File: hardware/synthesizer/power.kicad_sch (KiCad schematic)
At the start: 10 parts, among them U1 MAX40200ANS, U5 AP2112K-3.3

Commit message: update synthesizer
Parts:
- removed D5: BLUE_LED, symbol Device:LED
- removed R4: 1k, symbol Device:R
- added C12, C13: 1uF/16V, symbol Device:C
- added C14: 100uF/6.3V, symbol Device:C_Polarized
- added D8: Blue, symbol Device:LED
- added D9: Orange, symbol Device:LED
- added R13, R14: 1k, symbol Device:R
- added TP3: TestPoint, symbol Connector:TestPoint
- added U?: AP2112K-1.2, Package_TO_SOT_SMD:SOT-23-5, symbol Regulator_Linear:AP2112K-1.2
- D6: value RED_LED -> Red
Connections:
- net +5V: now also C12.1, R13.2, U?.1 (VIN), U?.3 (EN)
- net GND: now also C12.2, C13.2, C14.2, D8.1 (K), D9.1 (K), U?.2 (GND)
- new net: D9.2 (A), R14.2
- new net: D8.2 (A), R13.1
- new net +1.2V: C13.1, C14.1, R14.1, TP3.1, U?.5 (VOUT)
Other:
- note added: "5V -> 1.2V LDO"
- note added: "Power Led"

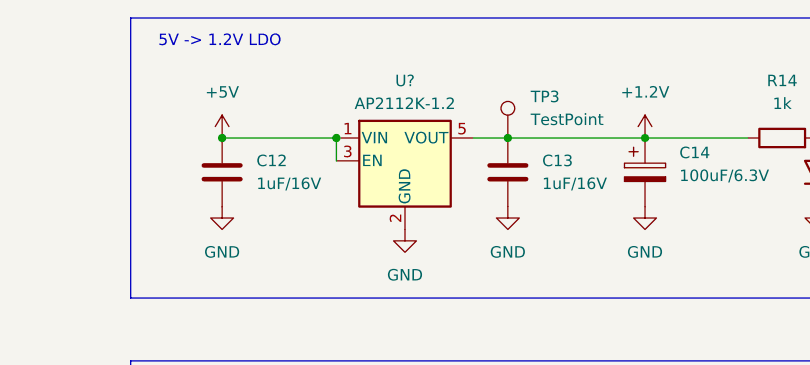
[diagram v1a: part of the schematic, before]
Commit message: finish ethernet jack
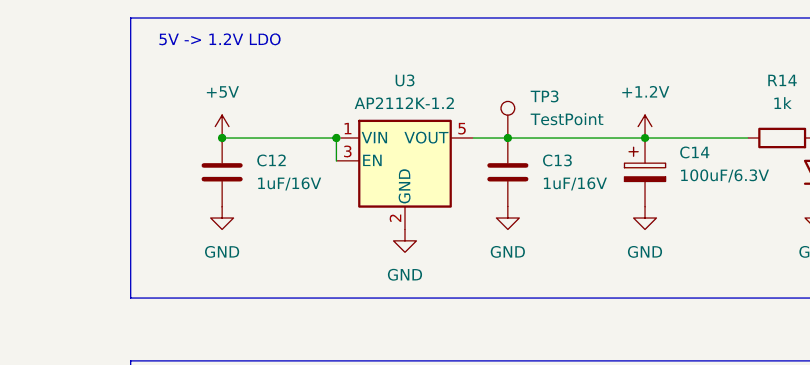
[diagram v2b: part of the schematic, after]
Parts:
- gave numbers to parts that had none: 1
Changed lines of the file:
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@@
 		(dnp no)
 		(fields_autoplaced yes)
-		(property "Reference" "U?"
+		(property "Reference" "U3"
 			(at 119.38 38.1 0)
 			(effects
@@
 			(project ""
 				(path "/f8740766-88d0-4c4d-b661-742f36f22c7b/9334189d-3538-4d48-bdb6-b549e4e68e82"
-					(reference "U?")
+					(reference "U3")
 					(unit 1)
 				)

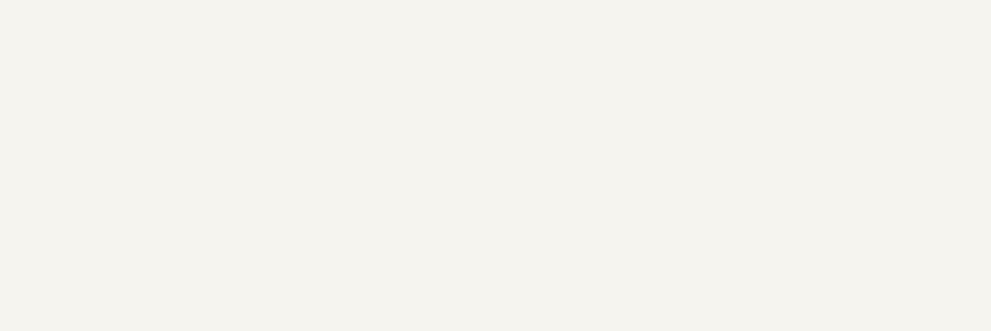
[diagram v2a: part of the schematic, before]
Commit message: add logo to every sheet
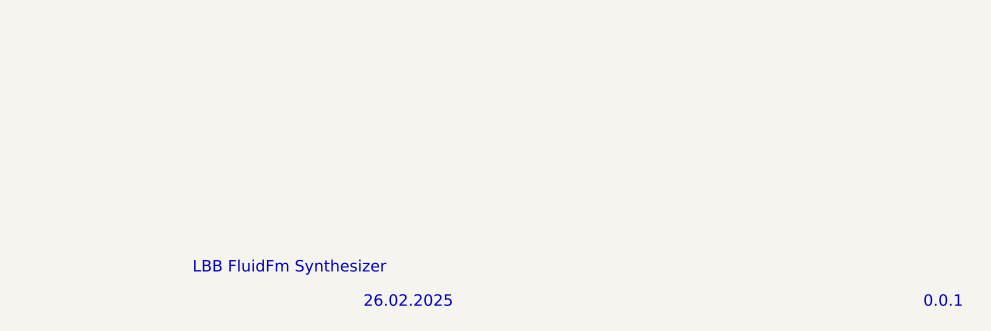
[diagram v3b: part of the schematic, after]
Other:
- note added: "0.0.1"
- note added: "26.02.2025"
- note added: "LBB FluidFm Synthesizer"

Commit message: improved pcb design
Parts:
- D6, D8, D9: footprint (none) -> LED_SMD:LED_0201_0603Metric
- R13, R14, R6: footprint (none) -> Resistor_SMD:R_0603_1608Metric
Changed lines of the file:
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@@
 			)
 		)
-		(property "Footprint" ""
+		(property "Footprint" "LED_SMD:LED_0201_0603Metric"
 			(at 165.1 86.36 0)
 			(effects
@@
 			)
 		)
-		(property "Footprint" ""
+		(property "Footprint" "Resistor_SMD:R_0603_1608Metric"
 			(at 161.29 84.328 90)
 			(effects
@@
 			)
 		)
-		(property "Footprint" ""
+		(property "Footprint" "LED_SMD:LED_0201_0603Metric"
 			(at 165.1 48.26 0)
 			(effects
@@
 			)
 		)
-		(property "Footprint" ""
+		(property "Footprint" "Resistor_SMD:R_0603_1608Metric"
 			(at 57.15 84.328 90)
 			(effects
@@
 			)
 		)
-		(property "Footprint" ""
+		(property "Footprint" "LED_SMD:LED_0201_0603Metric"
 			(at 49.53 87.63 0)
 			(effects
@@
 			)
 		)
-		(property "Footprint" ""
+		(property "Footprint" "Resistor_SMD:R_0603_1608Metric"
 			(at 161.29 46.228 90)
 			(effects

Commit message: improved pcb design
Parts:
- TP2, TP3: footprint (none) -> TestPoint:TestPoint_THTPad_1.0x1.0mm_Drill0.5mm
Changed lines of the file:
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@@
 			)
 		)
-		(property "Footprint" ""
+		(property "Footprint" "TestPoint:TestPoint_THTPad_1.0x1.0mm_Drill0.5mm"
 			(at 135.89 82.55 0)
 			(effects
@@
 			)
 		)
-		(property "Footprint" ""
+		(property "Footprint" "TestPoint:TestPoint_THTPad_1.0x1.0mm_Drill0.5mm"
 			(at 135.89 44.45 0)
 			(effects
